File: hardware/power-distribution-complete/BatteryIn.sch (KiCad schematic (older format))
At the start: 19 parts, among them J38 CTRL, J39 M6 Battery input, J40 M6 Battery input, Q17 Q_NMOS_SGD, Q18 Q_NMOS_SGD, Q19 Q_NMOS_SGD, Q20 Q_NMOS_SGD, Q21 Q_NMOS_SGD, Q22 Q_NMOS_SGD, U1 LTC4365TS8

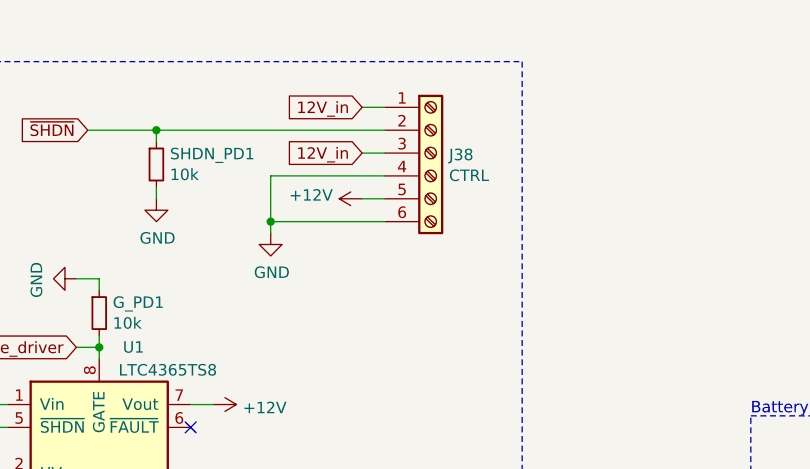
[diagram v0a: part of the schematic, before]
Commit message: Updated the power distribution schematic and pcb
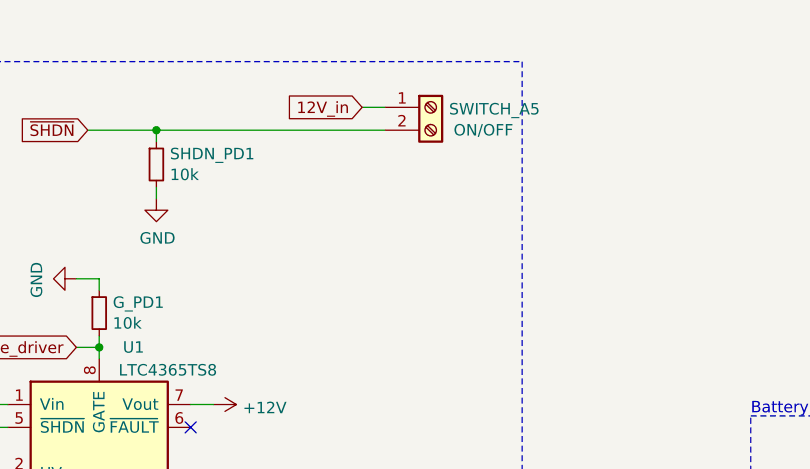
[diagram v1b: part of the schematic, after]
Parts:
- removed J38: CTRL, TerminalBlock_Phoenix:TerminalBlock_Phoenix_MKDS-1,5-6_1x06_P5.00mm_Horizontal, symbol Connector:Screw_Terminal_01x06
- added SWITCH_A5: ON/OFF, connectors:TerminalBlock_02_P5.00mm, symbol Connector:Screw_Terminal_01x02
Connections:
- net 12V_in: now also SWITCH_A5.1 (Pin_1)
- net ~SHDN: now also SWITCH_A5.2 (Pin_2)
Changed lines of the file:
@@
 	5900 2700 5550 2700
 NoConn ~ 7200 2500
-$Comp
-L Connector:Screw_Terminal_01x06 J38
-U 1 1 5F269231
-P 8250 1300
-F 0 "J38" H 8330 1292 50  0000 L CNN
-F 1 "CTRL" H 8330 1201 50  0000 L CNN
-F 2 "TerminalBlock_Phoenix:TerminalBlock_Phoenix_MKDS-1,5-6_1x06_P5.00mm_Horizontal" H 8250 1300 50  0001 C CNN
-F 3 "~" H 8250 1300 50  0001 C CNN
-	1    8250 1300
-	1    0    0    -1
-$EndComp
 Wire Wire Line
 	7950 1100 8050 1100
 Text GLabel 7950 1100 0    50   Input ~ 0
 12V_in
-Text GLabel 7950 1300 0    50   Input ~ 0
-12V_in
-Wire Wire Line
-	7550 1600 8050 1600
-Wire Wire Line
-	7950 1500 8050 1500
-Wire Wire Line
-	8050 1300 7950 1300
-Wire Wire Line
-	7550 1600 7550 1400
-Wire Wire Line
-	7550 1400 8050 1400
-Wire Wire Line
-	7550 1600 7550 1650
-Connection ~ 7550 1600
-$Comp
-L power:GND #PWR0100
-U 1 1 5F26DF10
-P 7550 1650
-F 0 "#PWR0100" H 7550 1400 50  0001 C CNN
-F 1 "GND" H 7555 1477 50  0000 C CNN
-F 2 "" H 7550 1650 50  0001 C CNN
-F 3 "" H 7550 1650 50  0001 C CNN
-	1    7550 1650
-	1    0    0    -1
-$EndComp
 Text Notes 5150 3600 0    50   ~ 0
 12.00 V - 434 Ohm\n11.75 V - 444 Ohm\n11.50 V - 454 Ohm\n11.25 V - 465 Ohm
@@
 $EndComp
 $Comp
-L power:+12V #PWR0101
-U 1 1 600B037F
-P 7950 1500
-F 0 "#PWR0101" H 7950 1350 50  0001 C CNN
-F 1 "+12V" V 7965 1628 50  0000 L CNN
-F 2 "" H 7950 1500 50  0001 C CNN
-F 3 "" H 7950 1500 50  0001 C CNN
-	1    7950 1500
-	0    -1   -1   0
+L Connector:Screw_Terminal_01x02 SWITCH_A?
+U 1 1 5FDC7140
+P 8250 1100
+AR Path="/5FDBC42A/5FDC7140" Ref="SWITCH_A?"  Part="1"
+AR Path="/600A69B6/5FDC7140" Ref="SWITCH_A5"  Part="1"
+F 0 "SWITCH_A5" H 8330 1092 50  0000 L CNN
+F 1 "ON/OFF" H 8350 1000 50  0000 L CNN
+F 2 "connectors:TerminalBlock_02_P5.00mm" H 8250 1100 50  0001 C CNN
+F 3 "~" H 8250 1100 50  0001 C CNN
+	1    8250 1100
+	1    0    0    -1
 $EndComp
 $EndSCHEMATC

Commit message: Power distribution complete first order
The board is finished and ordered.

Added TVS diode to protect the board from transients.
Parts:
- removed G_PD1: 10k, Resistor_SMD:R_0603_1608Metric, symbol Device:R_Small
- added D37, D38, D39: D_Small, diode:SMF-DO-219AB, symbol Device:D_Small
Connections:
- net 12V_in: now also D37.1 (K), D38.1 (K), D39.1 (K)
- net GND: now also D37.2 (A), D38.2 (A), D39.2 (A)
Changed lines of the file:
@@
 	1    0    0    -1
 $EndComp
-Wire Wire Line
-	7200 2400 7300 2400
 $Comp
 L Device:R_Small UV1
@@
 Text GLabel 6700 2150 0    50   Input ~ 0
 gate_driver
-$Comp
-L Device:R_Small G_PD1
-U 1 1 5F05F68F
-P 6800 2000
-F 0 "G_PD1" H 6859 2046 50  0000 L CNN
-F 1 "10k" H 6859 1955 50  0000 L CNN
-F 2 "Resistor_SMD:R_0603_1608Metric" H 6800 2000 50  0001 C CNN
-F 3 "~" H 6800 2000 50  0001 C CNN
-	1    6800 2000
-	1    0    0    -1
-$EndComp
-Wire Wire Line
-	6700 1850 6800 1850
-Wire Wire Line
-	6800 1850 6800 1900
-Wire Wire Line
-	6800 2100 6800 2150
 Wire Wire Line
 	6700 2150 6800 2150
-Connection ~ 6800 2150
 Wire Wire Line
 	6800 2150 6800 2200
-$Comp
-L power:GND #PWR096
-U 1 1 5F063FBA
-P 6700 1850
-F 0 "#PWR096" H 6700 1600 50  0001 C CNN
-F 1 "GND" H 6705 1677 50  0000 C CNN
-F 2 "" H 6700 1850 50  0001 C CNN
-F 3 "" H 6700 1850 50  0001 C CNN
-	1    6700 1850
-	0    1    1    0
-$EndComp
 Wire Wire Line
 	6400 2800 6250 2800
@@
 L power:+12V #PWR099
 U 1 1 600AD90F
-P 7300 2400
-F 0 "#PWR099" H 7300 2250 50  0001 C CNN
-F 1 "+12V" V 7315 2528 50  0000 L CNN
-F 2 "" H 7300 2400 50  0001 C CNN
-F 3 "" H 7300 2400 50  0001 C CNN
-	1    7300 2400
+P 7550 2400
+F 0 "#PWR099" H 7550 2250 50  0001 C CNN
+F 1 "+12V" V 7565 2528 50  0000 L CNN
+F 2 "" H 7550 2400 50  0001 C CNN
+F 3 "" H 7550 2400 50  0001 C CNN
+	1    7550 2400
 	0    1    1    0
 $EndComp
@@
 	1    0    0    -1
 $EndComp
+$Comp
+L Device:D_Small D?
+U 1 1 601B4417
+P 10100 3850
+AR Path="/5FEC946E/601B4417" Ref="D?"  Part="1"
+AR Path="/600A69B6/601B4417" Ref="D37"  Part="1"
+F 0 "D37" H 10100 4057 50  0000 C CNN
+F 1 "D_Small" H 10100 3966 50  0000 C CNN
+F 2 "diode:SMF-DO-219AB" V 10100 3850 50  0001 C CNN
+F 3 "~" V 10100 3850 50  0001 C CNN
+	1    10100 3850
+	0    1    1    0
+$EndComp
+Wire Wire Line
+	10100 4050 10100 4000
+Text GLabel 10050 3700 0    50   Input ~ 0
+12V_in
+Wire Wire Line
+	10050 3700 10100 3700
+Wire Wire Line
+	10100 3700 10100 3750
+$Comp
+L power:GND #PWR0107
+U 1 1 601B51B8
+P 10100 4050
+F 0 "#PWR0107" H 10100 3800 50  0001 C CNN
+F 1 "GND" H 10105 3877 50  0000 C CNN
+F 2 "" H 10100 4050 50  0001 C CNN
+F 3 "" H 10100 4050 50  0001 C CNN
+	1    10100 4050
+	1    0    0    -1
+$EndComp
+$Comp
+L Device:D_Small D?
+U 1 1 60240FA3
+P 10400 3850
+AR Path="/5FEC946E/60240FA3" Ref="D?"  Part="1"
+AR Path="/600A69B6/60240FA3" Ref="D38"  Part="1"
+F 0 "D38" H 10400 4057 50  0000 C CNN
+F 1 "D_Small" H 10400 3966 50  0000 C CNN
+F 2 "diode:SMF-DO-219AB" V 10400 3850 50  0001 C CNN
+F 3 "~" V 10400 3850 50  0001 C CNN
+	1    10400 3850
+	0    1    1    0
+$EndComp
+$Comp
+L Device:D_Small D?
+U 1 1 6024113E
+P 10700 3850
+AR Path="/5FEC946E/6024113E" Ref="D?"  Part="1"
+AR Path="/600A69B6/6024113E" Ref="D39"  Part="1"
+F 0 "D39" H 10700 4057 50  0000 C CNN
+F 1 "D_Small" H 10700 3966 50  0000 C CNN
+F 2 "diode:SMF-DO-219AB" V 10700 3850 50  0001 C CNN
+F 3 "~" V 10700 3850 50  0001 C CNN
+	1    10700 3850
+	0    1    1    0
+$EndComp
+Wire Wire Line
+	10700 3950 10700 4000
+Wire Wire Line
+	10700 4000 10400 4000
+Connection ~ 10100 4000
+Wire Wire Line
+	10100 4000 10100 3950
+Wire Wire Line
+	10400 4000 10400 3950
+Connection ~ 10400 4000
+Wire Wire Line
+	10400 4000 10100 4000
+Wire Wire Line
+	10400 3750 10400 3700
+Wire Wire Line
+	10400 3700 10100 3700
+Connection ~ 10100 3700
+Wire Wire Line
+	10400 3700 10700 3700
+Wire Wire Line
+	10700 3700 10700 3750
+Connection ~ 10400 3700
+Wire Wire Line
+	7200 2400 7550 2400
 $EndSCHEMATC

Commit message: Changed UV resistor.
The resistor now will make sure the battery is cut-off at
20 - 30% SoC.
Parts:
- UV2: value 470R -> 444R
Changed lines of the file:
@@
 P 5550 2850
 F 0 "UV2" H 5609 2896 50  0000 L CNN
-F 1 "470R" H 5609 2805 50  0000 L CNN
+F 1 "444R" H 5609 2805 50  0000 L CNN
 F 2 "Resistor_SMD:R_0603_1608Metric" H 5550 2850 50  0001 C CNN
 F 3 "~" H 5550 2850 50  0001 C CNN

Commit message: Added more resistor calculations.
Added how to get 11.1 V as UV.
This is below the voltage before the battery
is destroyed. An AGM is able to handle
a couple of these.
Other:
- note added: "8.2k and 360 gives 11.9 V\n10k and 470 gives 11.1 V"
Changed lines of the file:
@@
 Wire Wire Line
 	7200 2400 7550 2400
+Text Notes 5150 3800 0    50   ~ 0
+8.2k and 360 gives 11.9 V\n10k and 470 gives 11.1 V
 $EndSCHEMATC
